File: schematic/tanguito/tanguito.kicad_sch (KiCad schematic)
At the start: 5 parts, among them M1 DC Motor 12V, M2 DC Motor 12V, U1 L298N

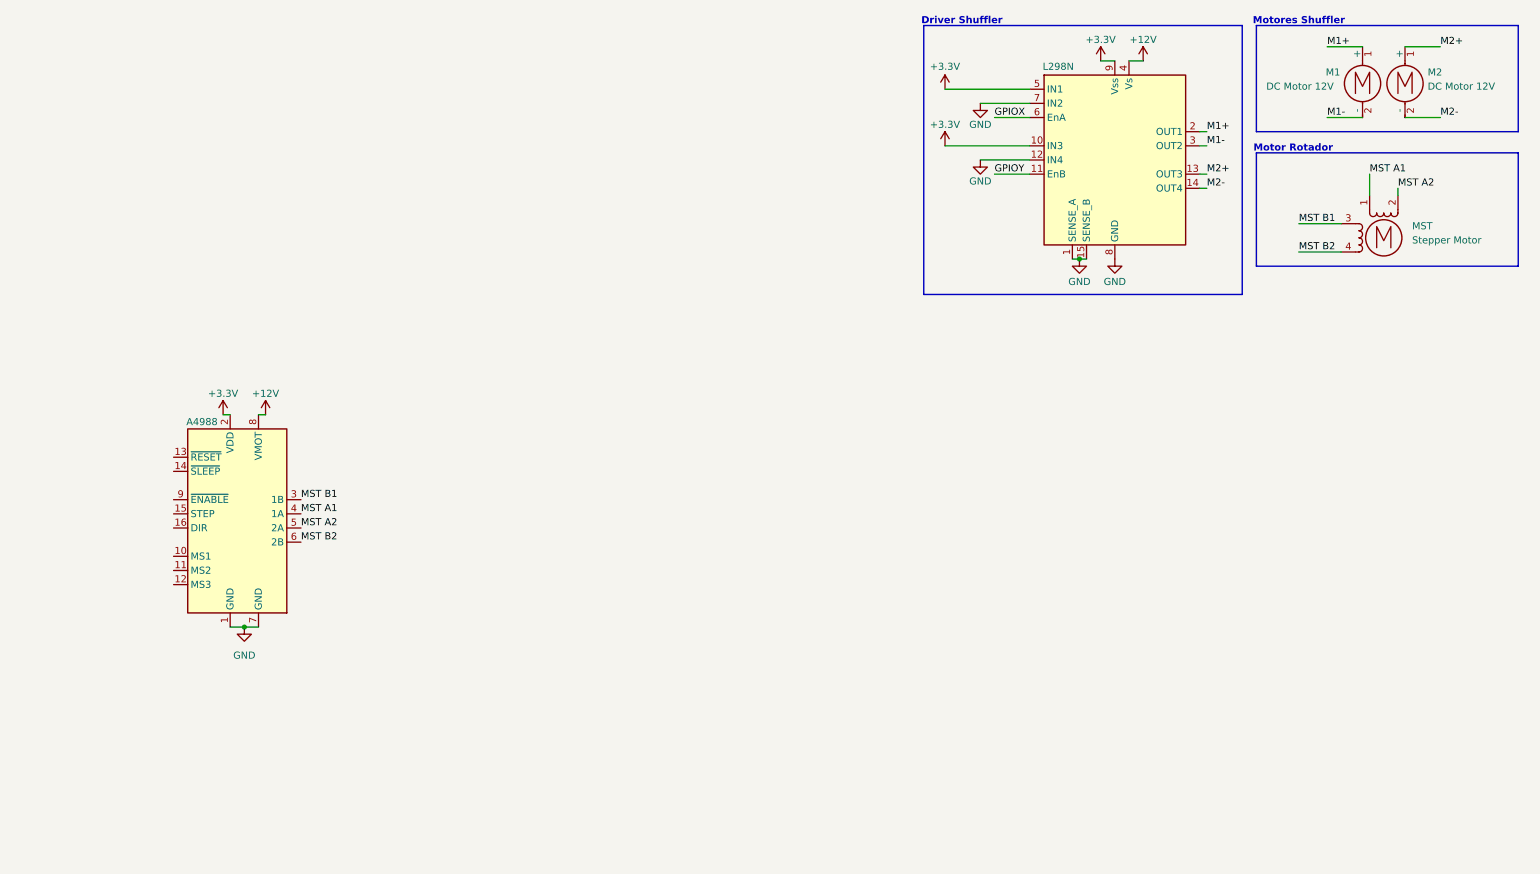
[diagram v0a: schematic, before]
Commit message: update: finished Driver Stepper schematic
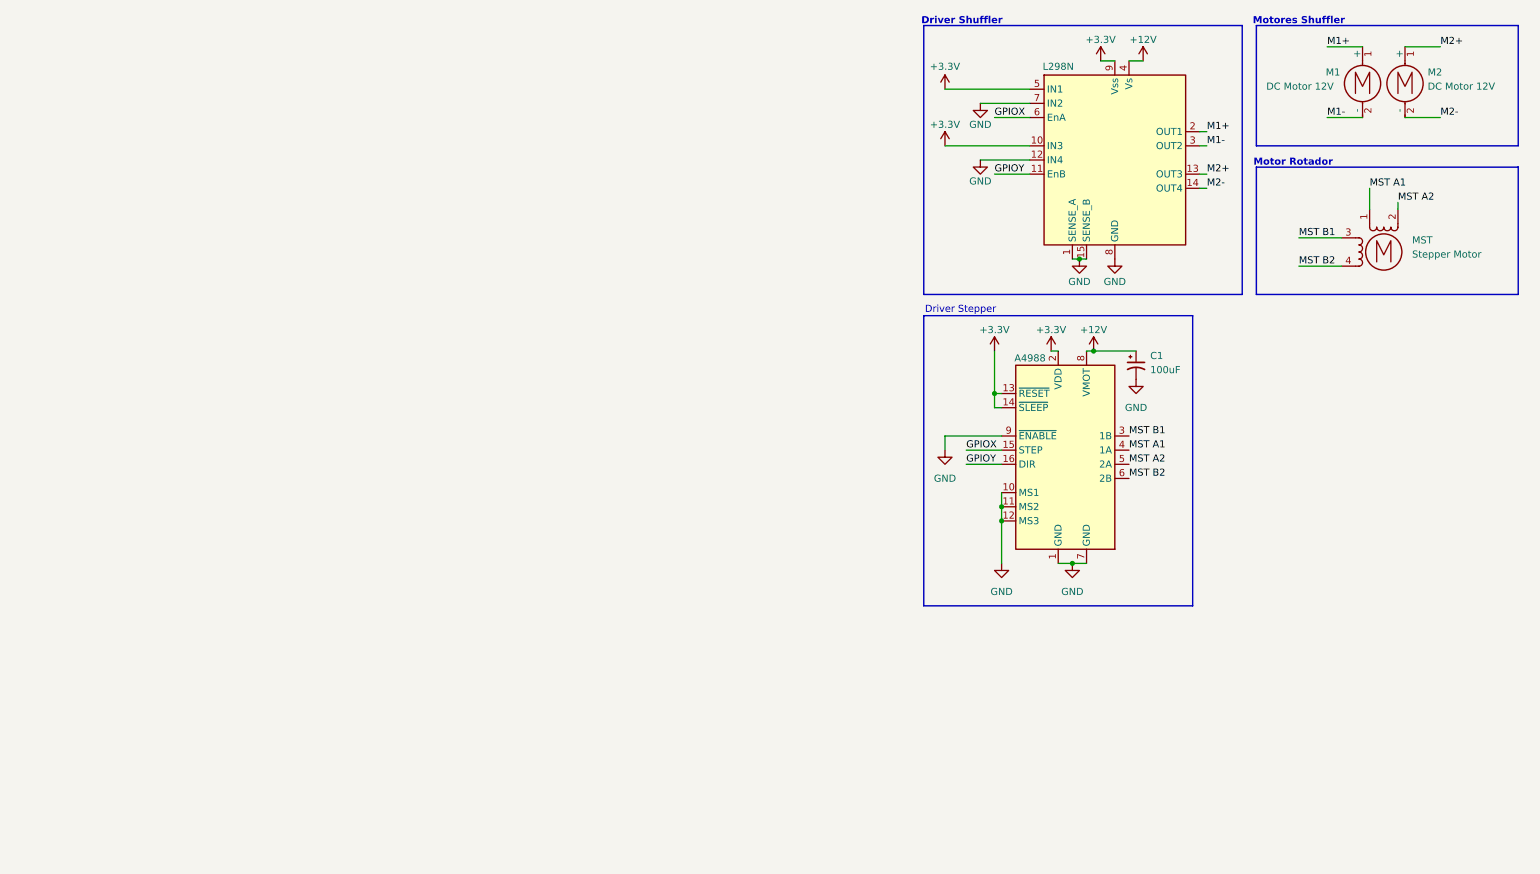
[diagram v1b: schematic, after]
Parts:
- added C1: 100uF, Package_LCC:PLCC-84_29.3x29.3mm_P1.27mm, symbol Device:C_Polarized_Small_US
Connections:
- net +12V: now also C1.1
- net +3.3V: now also A1.13 (~{RESET}), A1.14 (~{SLEEP})
- net GND: now also A1.10 (MS1), A1.11 (MS2), A1.12 (MS3), A1.9 (~{ENABLE}), C1.2
- net GPIOX: now also A1.15 (STEP)
- net GPIOY: now also A1.16 (DIR)
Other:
- note added: "Driver Stepper"
- moved on the sheet: MST

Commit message: feat: freertos eedu-ciaa incorporation and various tasks, INCOMPLETE
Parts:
- added J1: Barrel_Jack, Package_DFN_QFN:QFN-40-1EP_6x6mm_P0.5mm_EP4.6x4.6mm, symbol Connector:Barrel_Jack
- added U1, U2: (no value), Connector:Tag-Connect_TC2030-IDC-FP_2x03_P1.27mm_Vertical, symbol tanguito:EDU-CIAA
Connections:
- net +12V: now also J1.1
- net +3.3V: no longer U1.10 (IN3), U1.5 (IN1), U1.9 (Vss)
- net GND: now also J1.2
- net GPIOX renamed GPIO0
- net GPIO0: now also U2.29 (GPIO0); no longer A1.15 (STEP)
- net GPIOY renamed GPIO1
- net GPIO1: now also U2.32 (GPIO1); no longer A1.16 (DIR)
- new net +5V: U1.10 (IN3), U1.5 (IN1)
- new net GPIO2: A1.15 (STEP), U2.31 (GPIO2)
- new net GPIO3: A1.16 (DIR), U2.34 (GPIO3)
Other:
- note added: "Alimentación 12V"
- note added: "EDU-CIAA"
- moved on the sheet: C1, M1, M2, MST

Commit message: upload: schematic
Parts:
- added HW133AF: (no value), symbol tanguito:HW133AF
- added LCD1: (no value), symbol tanguito:LCD
- added M3: DC Motor 12V, Module:Maple_Mini, symbol Motor:Motor_DC
- added M4: DC Motor 12V, symbol Motor:Motor_DC
- added U3: L298N, Package_TO_SOT_THT:TO-220-15_P2.54x5.08mm_StaggerOdd_Lead4.58mm_Vertical, symbol Driver_Motor:L298N
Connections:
- net +12V: now also HW133AF. (VOUT-), U3.4 (Vs)
- net +3.3V: now also HW133AF. (VOUT-)
- net +5V: now also LCD1. (SCL); no longer U1.10 (IN3), U1.5 (IN1)
- net GND: now also U1.10 (IN3), HW133AF. (VOUT-), LCD1. (SCL), U3.10 (IN3), U3.7 (IN2), U3.8 (GND); no longer U1.1 (SENSE_A), U1.12 (IN4), U1.15 (SENSE_B)
- net GPIO0: now also U1.5 (IN1), U3.5 (IN1); no longer U1.6 (EnA)
- net GPIO1: now also U1.12 (IN4), U3.12 (IN4); no longer U1.11 (EnB)
- net M1+: now also M3.1 (+), U3.2 (OUT1)
- net M1-: now also M3.2 (-), U3.3 (OUT2)
- net M2+: now also M4.1 (+), U3.13 (OUT3)
- net M2-: now also M4.2 (-), U3.14 (OUT4)
- net I2C_SDA: now reaches U1.19 (I2C_SCA)
- net I2C_SDA: now also LCD1. (SCL)
- net I2C_SCL: now reaches U1.21 (I2C_SCL)
- net I2C_SCL: now also LCD1. (SCL)
- net PWM0: now reaches U1.36 (T_FL1)
- net PWM0: now also U1.6 (EnA), U3.6 (EnA)
- net PWM3: now reaches U1.37 (T_FL2)
- net PWM3: now also U1.11 (EnB), U3.11 (EnB)
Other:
- note added: "Alimentación 3.3V (Será mejor 5v?)"
- note added: "Display LCD"
- note added: "Driver Dealer"
- note added: "Motores Delaer (supongo que asi pero solo 1)"
- moved on the sheet: C1, M1, M2, MST

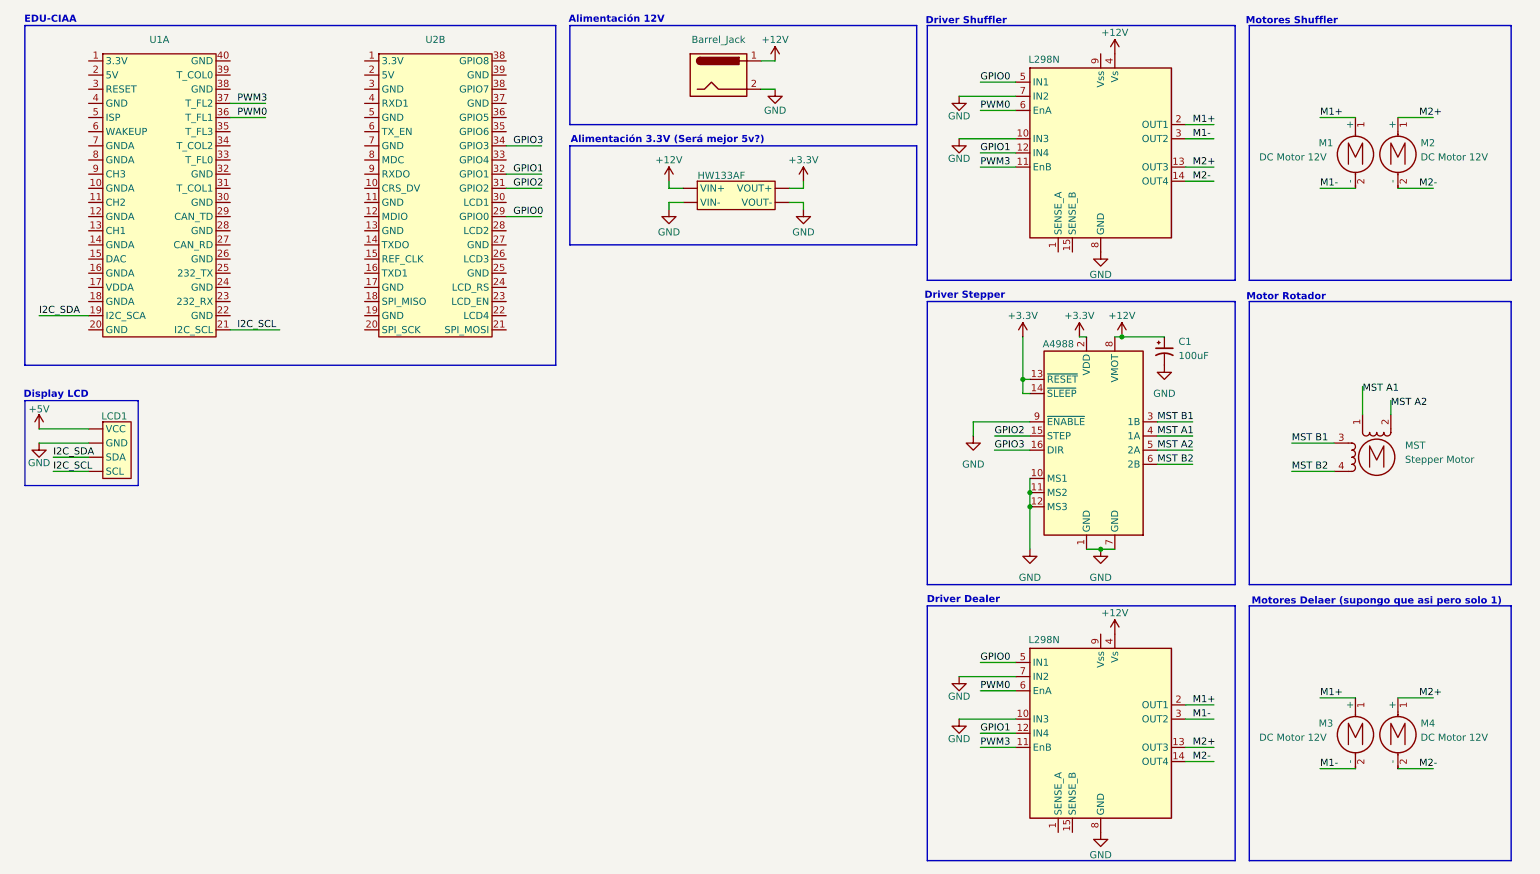
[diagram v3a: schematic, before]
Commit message: updated schemtaic
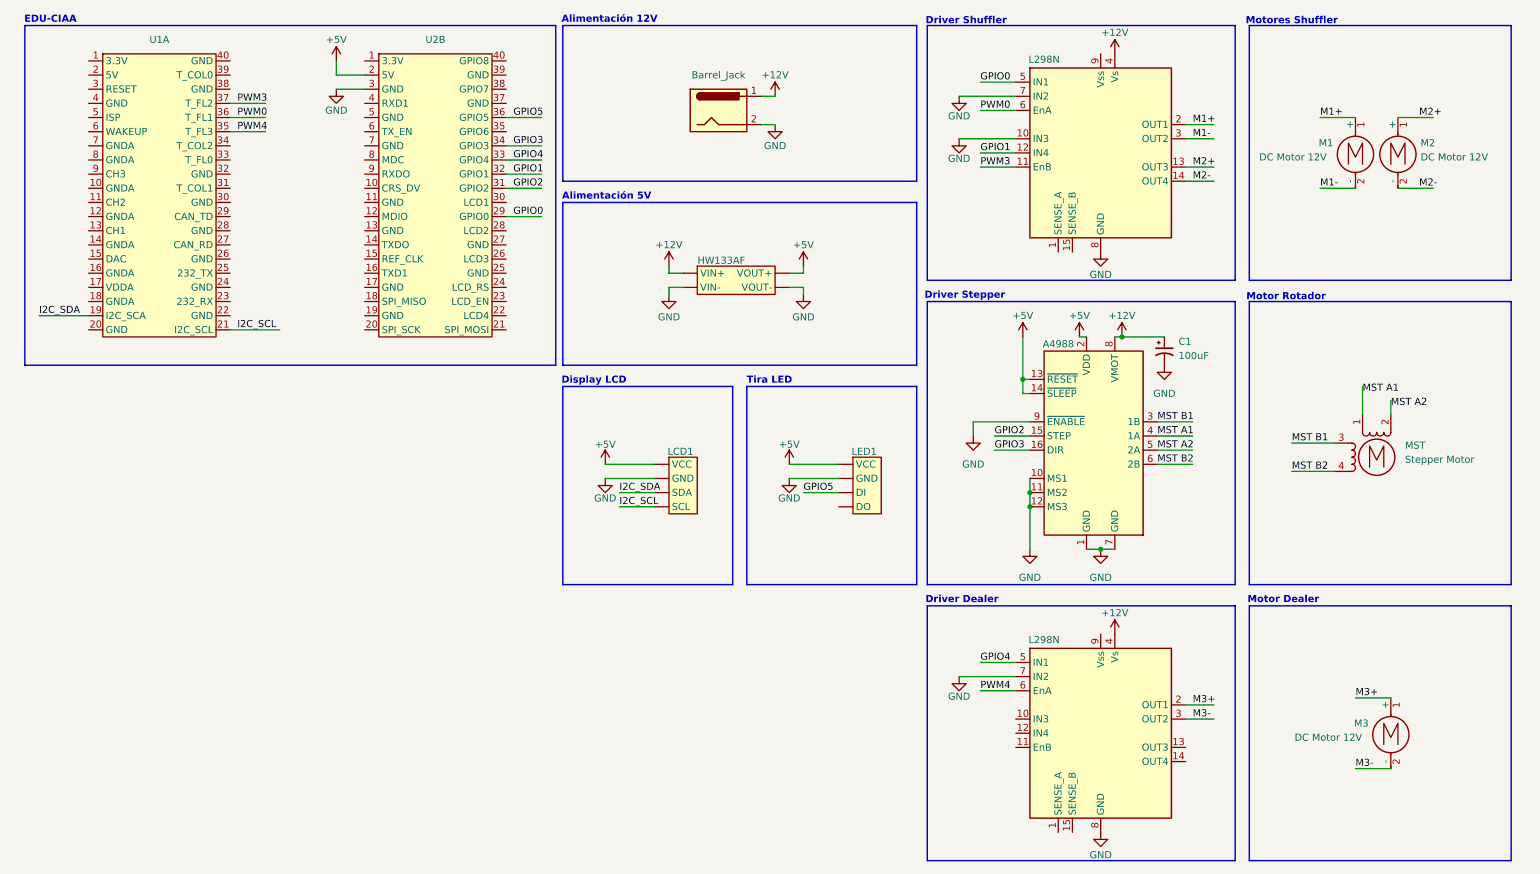
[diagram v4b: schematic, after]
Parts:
- removed M4: DC Motor 12V, symbol Motor:Motor_DC
- added LED1: (no value), symbol tanguito:LED
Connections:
- net +5V: now also A1.13 (~{RESET}), A1.14 (~{SLEEP}), A1.2 (VDD), HW133AF. (VOUT-), U2.2 (5V), LED1. (DO)
- net GND: now also U2.3 (GND), LED1. (DO); no longer U3.10 (IN3)
- net GPIO0: no longer U3.5 (IN1)
- net GPIO1: no longer U3.12 (IN4)
- net M1+: no longer M3.1 (+), U3.2 (OUT1)
- net M1-: no longer M3.2 (-), U3.3 (OUT2)
- net M2+: no longer U3.13 (OUT3)
- net M2-: no longer U3.14 (OUT4)
- net PWM0: no longer U3.6 (EnA)
- net PWM3: no longer U3.11 (EnB)
- net GPIO4: now reaches U2.33 (GPIO4)
- net GPIO4: now also U3.5 (IN1)
- net GPIO5: now reaches U2.36 (GPIO5)
- net GPIO5: now also LED1. (DO)
- net PWM4: now reaches U1.35 (T_FL3)
- net PWM4: now also U3.6 (EnA)
- removed net +3.3V: A1.13 (~{RESET}), A1.14 (~{SLEEP}), A1.2 (VDD), HW133AF. (VOUT-)
- new net M3+: M3.1 (+), U3.2 (OUT1)
- new net M3-: M3.2 (-), U3.3 (OUT2)
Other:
- note added: "Alimentación 5V"
- note added: "Motor Dealer"
- note added: "Tira LED"
- note removed: "Alimentación 3.3V (Será mejor 5v?)"
- note removed: "Motores Delaer (supongo que asi pero solo 1)"
- moved on the sheet: HW133AF, LCD1, M3

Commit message: esquematico actualizado para poder hacer la PCB y arranque de la PCB separando las 2 tiras de conectores 2x20 para que cumplan con las dimensiones de la EDU-CIAA
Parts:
- removed U2: (no value), Connector:Tag-Connect_TC2030-IDC-FP_2x03_P1.27mm_Vertical, symbol tanguito:EDU-CIAA
- added P2: (no value), Connector_PinHeader_2.54mm:PinHeader_2x20_P2.54mm_Vertical, symbol tanguito:EDU-CIAA
- C1: footprint Package_LCC:PLCC-84_29.3x29.3mm_P1.27mm -> Capacitor_THT:CP_Radial_D8.0mm_P3.50mm
- J1: footprint Package_DFN_QFN:QFN-40-1EP_6x6mm_P0.5mm_EP4.6x4.6mm -> TerminalBlock:TerminalBlock_MaiXu_MX126-5.0-02P_1x02_P5.00mm
- LCD1, LED1: footprint (none) -> Connector_PinHeader_1.00mm:PinHeader_1x04_P1.00mm_Vertical
- M1: footprint Module:Maple_Mini -> (none)
- M2: renamed from M3; footprint Module:Maple_Mini -> (none)
- MST1: renamed from MST; footprint (none) -> Connector_PinHeader_1.00mm:PinHeader_1x04_P1.00mm_Vertical
- P1: renamed from U1; footprint Connector:Tag-Connect_TC2030-IDC-FP_2x03_P1.27mm_Vertical -> Connector_PinHeader_2.54mm:PinHeader_2x20_P2.54mm_Vertical
- renumbered HW133AF to HW133AF1, M2 to M3, U1 to U2
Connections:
- net +12V: now also HW133AF1.1 (VIN+); no longer HW133AF1. (VOUT-)
- net +5V: now also HW133AF1.3 (VOUT+), LCD1.1 (VCC), LED1.1 (VCC), P2.2 (5V); no longer HW133AF1. (VOUT-), LCD1. (SCL), LED1. (DO)
- net GND: now also HW133AF1.2 (VIN-), HW133AF1.4 (VOUT-), LCD1.2 (GND), LED1.2 (GND), P2.3 (GND); no longer HW133AF1. (VOUT-), LCD1. (SCL), LED1. (DO)
- net GPIO0: now also P2.29 (GPIO0)
- net GPIO1: now also P2.32 (GPIO1)
- net GPIO2: now also P2.31 (GPIO2)
- net GPIO3: now also P2.34 (GPIO3)
- net GPIO4: now also P2.33 (GPIO4)
- net GPIO5: now also LED1.3 (DI), P2.36 (GPIO5); no longer LED1. (DO)
- net I2C_SCL: now also LCD1.4 (SCL); no longer LCD1. (SCL)
- net I2C_SDA: now also LCD1.3 (SDA); no longer LCD1. (SCL)
- net PWM0: no longer P1.36 (T_FL1)
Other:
- moved on the sheet: P1A
